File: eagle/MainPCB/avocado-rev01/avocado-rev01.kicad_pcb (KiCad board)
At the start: 4 copper layers, 61.5 x 59.8 mm, 110 parts, among them J1 10118194-0001LF, J3 0475710001, P2 camconn, U1 V3S, U2 AP65111A, U3 AP65111A, U4 AP65111A, U5 XC6206P302MR, X1 XTAL3.2X2, X2 XTAL5X1.9

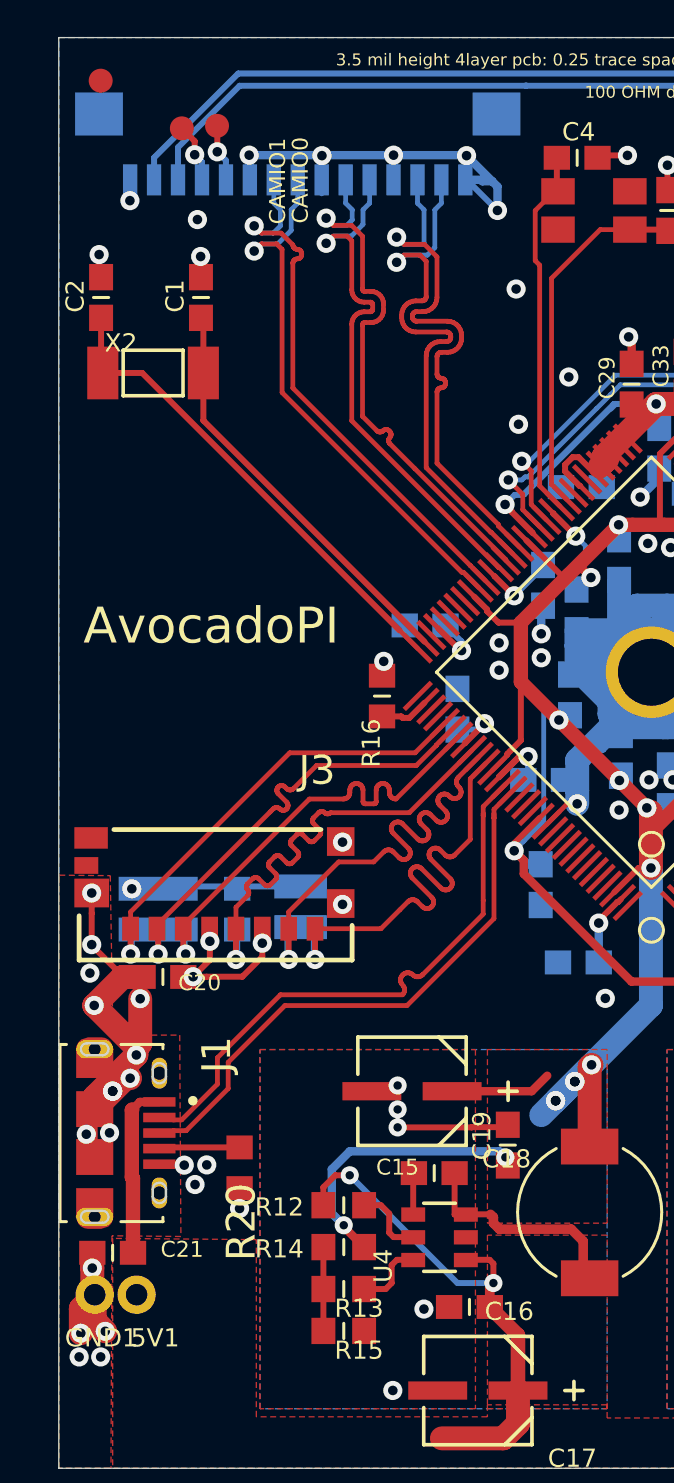
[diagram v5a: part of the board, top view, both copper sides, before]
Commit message: updated decoupling vias
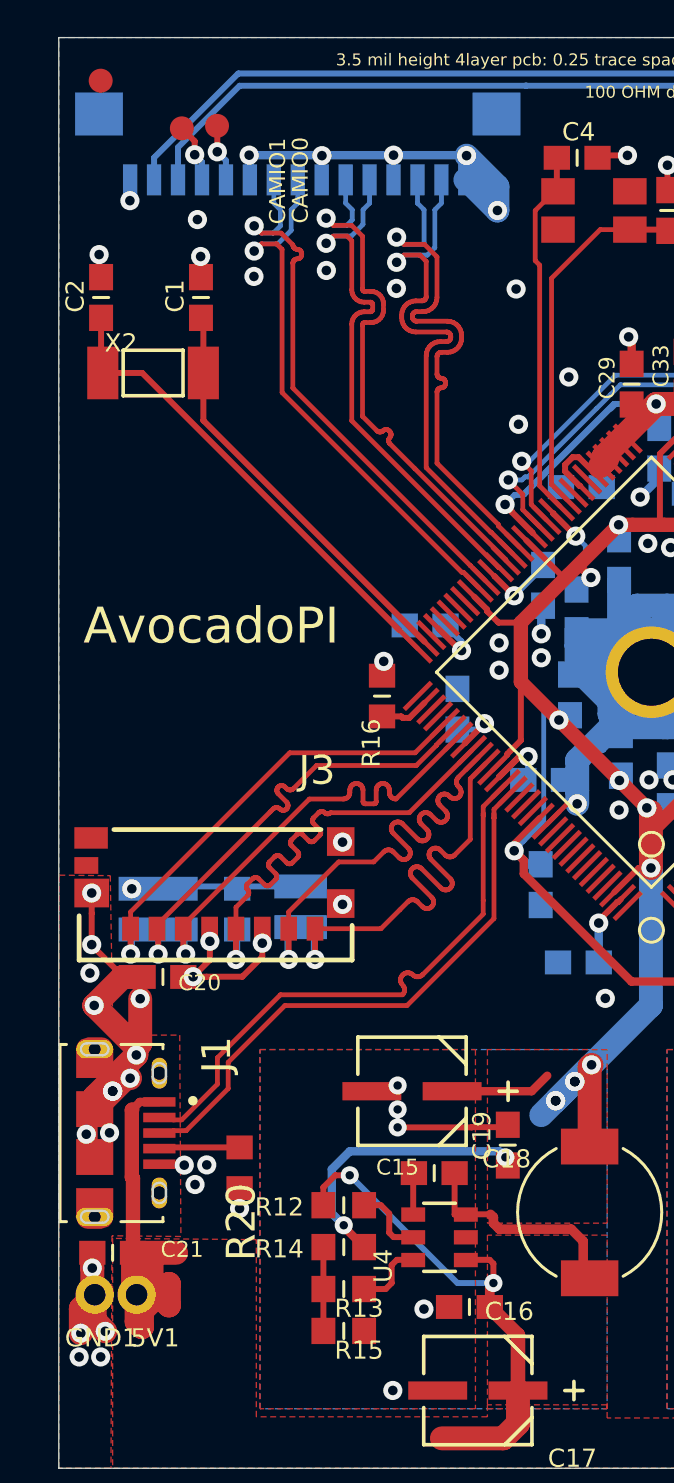
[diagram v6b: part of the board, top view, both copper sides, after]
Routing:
- net VCC: track 67.7 -> 78.4 mm
- net GND: track 150.5 -> 149.6 mm, vias 88 -> 91
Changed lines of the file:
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@@
-(kicad_pcb (version 20171130) (host pcbnew "(6.0.0-rc1-dev-1027-g90233e5ec)")
+(kicad_pcb (version 20171130) (host pcbnew "(5.0.2)-1")
   (general
     (thickness 1.6)
     (drawings 7)
-    (tracks 1809)
+    (tracks 1819)
     (zones 0)
     (modules 110)
@@
     (zone_45_only no)
     (trace_min 0.2)
+    (segment_width 0.2)
+    (edge_width 0.05)
     (via_size 0.8)
     (via_drill 0.4)
@@
     (uvia_min_size 0.2)
     (uvia_min_drill 0.1)
-    (edge_width 0.05)
-    (segment_width 0.2)
     (pcb_text_width 0.3)
     (pcb_text_size 1.5 1.5)
@@
   (via (at 135.85 85) (size 0.8) (drill 0.4) (layers Top Bottom) (net 1))
   (via (at 122.54 82.1) (size 0.8) (drill 0.4) (layers Top Bottom) (net 1))
-  (segment (start 127.73 80.44) (end 127.73 81) (width 0.25) (layer Bottom) (net 1))
   (segment (start 133.78 80.39) (end 133.73 80.44) (width 0.25) (layer Bottom) (net 1))
   (segment (start 133.78 79.43) (end 133.78 80.39) (width 0.25) (layer Bottom) (net 1))
-  (segment (start 133.79 80.44) (end 135.07 81.72) (width 0.25) (layer Bottom) (net 1))
-  (segment (start 133.73 80.44) (end 133.79 80.44) (width 0.25) (layer Bottom) (net 1))
   (segment (start 130.75 79.43) (end 130.73 79.41) (width 0.25) (layer Bottom) (net 1))
   (segment (start 133.78 79.43) (end 130.75 79.43) (width 0.25) (layer Bottom) (net 1))
@@
   (segment (start 133.76 79.41) (end 133.78 79.43) (width 0.35) (layer Bottom) (net 1))
   (segment (start 124.7 79.41) (end 133.76 79.41) (width 0.35) (layer Bottom) (net 1))
-  (segment (start 135.07 80.72) (end 135.07 81.72) (width 0.35) (layer Bottom) (net 1))
   (segment (start 134.44 80.5) (end 134.85 80.5) (width 0.35) (layer Bottom) (net 1))
-  (segment (start 134.38 80.44) (end 134.44 80.5) (width 0.35) (layer Bottom) (net 1))
-  (segment (start 133.73 80.44) (end 134.38 80.44) (width 0.35) (layer Bottom) (net 1))
-  (segment (start 133.78 79.43) (end 134.85 80.5) (width 0.35) (layer Bottom) (net 1))
   (segment (start 134.85 80.5) (end 135.07 80.72) (width 0.35) (layer Bottom) (net 1))
   (segment (start 141.825 92.895) (end 141.03 93.69) (width 0.35) (layer Bottom) (net 1))
@@
   (segment (start 158.925 112.9) (end 157.5 112.9) (width 0.35) (layer Top) (net 1))
   (via (at 156.15 112.825) (size 0.8) (drill 0.4) (layers Top Bottom) (net 1))
+  (via (at 130.85 84.975) (size 0.8) (drill 0.4) (layers Top Bottom) (net 1))
+  (via (at 127.925 84.225) (size 0.8) (drill 0.4) (layers Top Bottom) (net 1))
+  (via (at 124.9 84.475) (size 0.8) (drill 0.4) (layers Top Bottom) (net 1))
+  (segment (start 135.07 80.72) (end 133.78 79.43) (width 1) (layer Bottom) (net 1))
+  (segment (start 135.07 81.72) (end 135.07 80.72) (width 1) (layer Bottom) (net 1))
+  (segment (start 133.79 80.44) (end 135.07 81.72) (width 1) (layer Bottom) (net 1))
+  (segment (start 133.73 80.44) (end 133.79 80.44) (width 1) (layer Bottom) (net 1))
   (segment (start 145.8011 122.5136) (end 146.3011 122.0136) (width 0.25) (layer Top) (net 2))
   (via (at 146.9011 122.0136) (size 0.7564) (drill 0.35) (layers Top Bottom) (net 2))
@@
   (segment (start 171.9275 132.3846) (end 171.2621 133.05) (width 1) (layer Top) (net 2))
   (segment (start 171.9275 131.0036) (end 171.9275 132.3846) (width 1) (layer Top) (net 2))
+  (segment (start 119.85 126.85) (end 120 127) (width 1) (layer Top) (net 2))
+  (segment (start 119.85 125.25) (end 119.85 126.85) (width 1) (layer Top) (net 2))
+  (segment (start 120 128.13137) (end 120.225 128.35637) (width 1) (layer Top) (net 2))
+  (segment (start 120 127) (end 120 128.13137) (width 1) (layer Top) (net 2))
+  (segment (start 120.225 128.35637) (end 120.225 127.675) (width 1) (layer Top) (net 2))
+  (segment (start 120.225 127.675) (end 121.35 126.55) (width 1) (layer Top) (net 2))
+  (segment (start 121.35 126.55) (end 121.35 127.45) (width 1) (layer Top) (net 2))
+  (segment (start 121.35 127.45) (end 120.625 126.725) (width 1) (layer Top) (net 2))
+  (segment (start 120.625 126.725) (end 120.625 125.325) (width 1) (layer Top) (net 2))
+  (segment (start 119.85 125.25) (end 121.65 125.25) (width 1) (layer Top) (net 2))
   (via (at 122.36 113.72) (size 0.8) (drill 0.4) (layers Top Bottom) (net 3))
   (segment (start 165.5011 125.0136) (end 164.6511 124.1636) (width 0.35) (layer Top) (net 3))
@@
   (segment (start 122.425428 78.825428) (end 121.89 78.29) (width 0.25) (layer Top) (net 18))
   (segment (start 122.425428 79.39188) (end 122.425428 78.825428) (width 0.25) (layer Top) (net 18))
-  (via (at 138.34 95.32) (size 0.8) (drill 0.4) (layers Top Bottom) (net 68))
-  (segment (start 137.399881 94.356796) (end 137.399881 94.379881) (width 0.25) (layer Top) (net 68))
-  (segment (start 137.399881 94.379881) (end 138.34 95.32) (width 0.25) (layer Top) (net 68))
-  (via (at 135.768795 108.461323) (size 0.8) (drill 0.4) (layers Top Bottom) (net 68))
-  (segment (start 136.834195 107.084718) (end 135.768795 108.150118) (width 0.25) (layer Top) (net 68))
-  (segment (start 135.768795 108.150118) (end 135.768795 108.461323) (width 0.25) (layer Top) (net 68))
-  (segment (start 138.739999 95.719999) (end 138.739999 96.060001) (width 0.2) (layer Bottom) (net 68))
-  (segment (start 138.34 95.32) (end 138.739999 95.719999) (width 0.2) (layer Bottom) (net 68))
-  (segment (start 138.739999 96.060001) (end 136.2 98.6) (width 0.2) (layer Bottom) (net 68))
-  (segment (start 136.2 98.6) (end 136.2 101.5) (width 0.2) (layer Bottom) (net 68))
-  (segment (start 136.168794 108.061324) (end 135.768795 108.461323) (width 0.2) (layer Bottom) (net 68))
-  (segment (start 137.002401 107.227717) (end 136.168794 108.061324) (width 0.2) (layer Bottom) (net 68))
-  (segment (start 137.002401 102.302401) (end 137.002401 107.227717) (width 0.2) (layer Bottom) (net 68))
-  (segment (start 136.2 101.5) (end 137.002401 102.302401) (width 0.2) (layer Bottom) (net 68))
   (segment (start 131.05 102.85) (end 130.25 102.85) (width 0.25) (layer Top) (net 19))
   (segment (start 131.112787 102.912787) (end 131.05 102.85) (width 0.25) (layer Top) (net 19))
@@
   (segment (start 131.833099 113.707929) (end 131.891839 113.679642) (width 0.2) (layer Top) (net 67))
   (segment (start 131.891839 113.679642) (end 131.942811 113.638992) (width 0.2) (layer Top) (net 67))
+  (via (at 138.34 95.32) (size 0.8) (drill 0.4) (layers Top Bottom) (net 68))
+  (segment (start 137.399881 94.356796) (end 137.399881 94.379881) (width 0.25) (layer Top) (net 68))
+  (segment (start 137.399881 94.379881) (end 138.34 95.32) (width 0.25) (layer Top) (net 68))
+  (via (at 135.768795 108.461323) (size 0.8) (drill 0.4) (layers Top Bottom) (net 68))
+  (segment (start 136.834195 107.084718) (end 135.768795 108.150118) (width 0.25) (layer Top) (net 68))
+  (segment (start 135.768795 108.150118) (end 135.768795 108.461323) (width 0.25) (layer Top) (net 68))
+  (segment (start 138.739999 95.719999) (end 138.739999 96.060001) (width 0.2) (layer Bottom) (net 68))
+  (segment (start 138.34 95.32) (end 138.739999 95.719999) (width 0.2) (layer Bottom) (net 68))
+  (segment (start 138.739999 96.060001) (end 136.2 98.6) (width 0.2) (layer Bottom) (net 68))
+  (segment (start 136.2 98.6) (end 136.2 101.5) (width 0.2) (layer Bottom) (net 68))
+  (segment (start 136.168794 108.061324) (end 135.768795 108.461323) (width 0.2) (layer Bottom) (net 68))
+  (segment (start 137.002401 107.227717) (end 136.168794 108.061324) (width 0.2) (layer Bottom) (net 68))
+  (segment (start 137.002401 102.302401) (end 137.002401 107.227717) (width 0.2) (layer Bottom) (net 68))
+  (segment (start 136.2 101.5) (end 137.002401 102.302401) (width 0.2) (layer Bottom) (net 68))
   (segment (start 157.6 114.8) (end 157.45 114.65) (width 0.35) (layer Top) (net 68))
   (segment (start 158.925 114.8) (end 157.6 114.8) (width 0.35) (layer Top) (net 68))
@@
     (polygon
       (pts
-        (xy 121.71 81.1) (xy 136.05 81.0775) (xy 136.99 82.8425) (xy 136.73 85.795) (xy 121.66 85.76)
+        (xy 121.71 81.1) (xy 136.05 81.0775) (xy 136.99 82.8425) (xy 136.73 86.3775) (xy 121.66 86.3425)
       )
     )
@@
     (polygon
       (pts
-        (xy 136.58 85.83) (xy 122.13 85.65) (xy 121.95 87.13) (xy 136.6 87.3) (xy 136.58 85.81)
+        (xy 136.58 86.45) (xy 122.13 86.27) (xy 121.95 87.13) (xy 136.6 87.3) (xy 136.58 85.81)
       )
     )

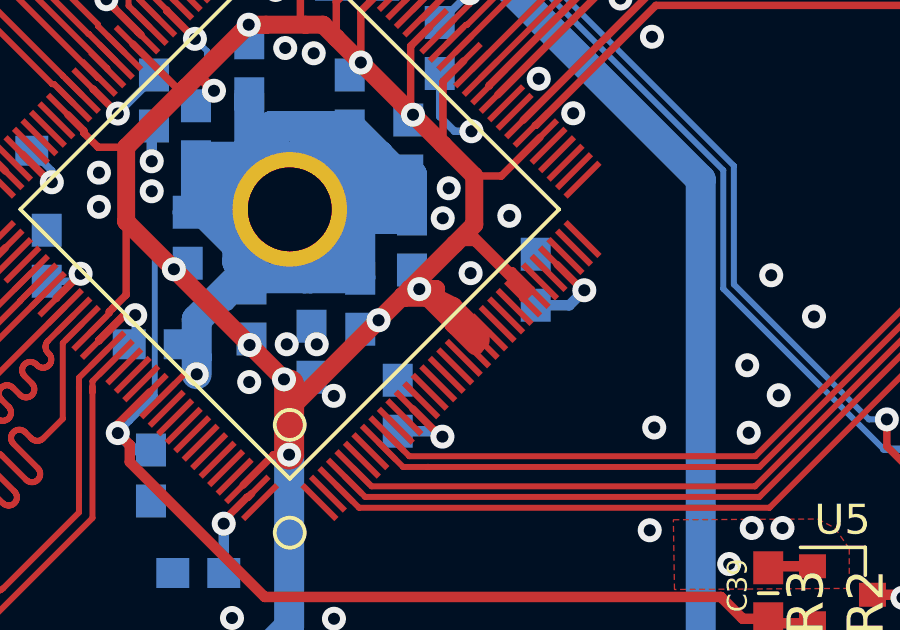
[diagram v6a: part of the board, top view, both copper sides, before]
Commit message: update keepout area
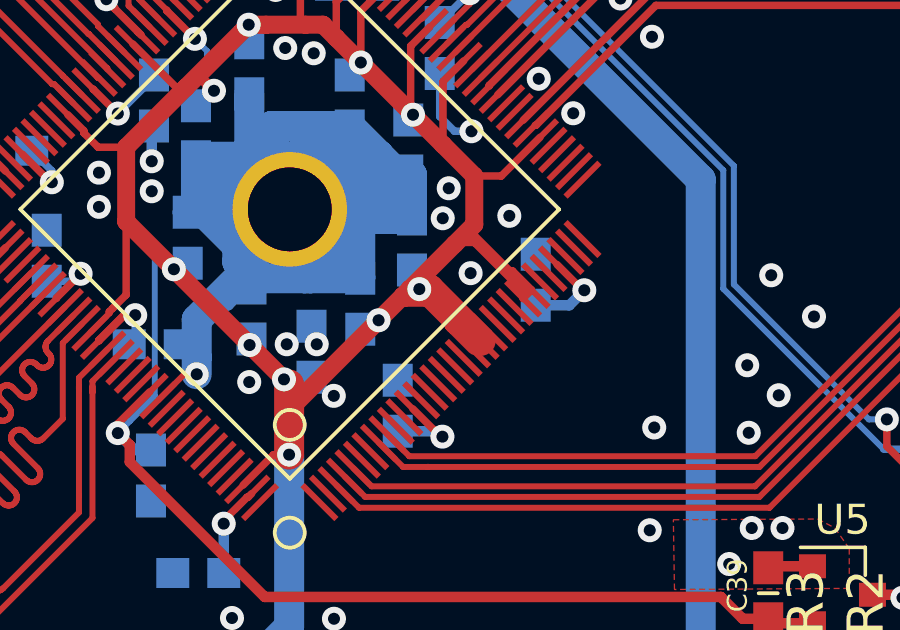
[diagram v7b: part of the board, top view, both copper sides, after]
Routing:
- net 1V2: track 126.6 -> 128.2 mm
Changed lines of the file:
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@@
   (segment (start 147.865061 105.146241) (end 146.95 104.23118) (width 0.6) (layer Top) (net 5))
   (segment (start 146.95 104.822743) (end 146.95 104.791554) (width 0.6) (layer Top) (net 5))
-  (segment (start 146.380374 103.661554) (end 145.82 103.661554) (width 0.6) (layer Top) (net 5))
   (segment (start 145.82 103.661554) (end 145.5 103.661554) (width 0.6) (layer Top) (net 5))
   (segment (start 145.328446 103.95) (end 145.27 103.891554) (width 0.6) (layer Top) (net 5))
@@
   (segment (start 145.61 97.848446) (end 145.61 97.848446) (width 0.25) (layer Top) (net 5))
   (via (at 145.61 97.848446) (size 0.8) (drill 0.4) (layers Top Bottom) (net 5))
-  (segment (start 145.82 103.661554) (end 146.380374 103.661554) (width 0.6) (layer Top) (net 5))
   (via (at 145.82 103.661554) (size 0.8) (drill 0.4) (layers Top Bottom) (net 5))
   (segment (start 144.461554 104.7) (end 145.27 103.891554) (width 0.6) (layer Top) (net 5))
@@
   (segment (start 142.155 106.67) (end 142.225 106.6) (width 0.25) (layer Bottom) (net 5))
   (segment (start 141.308446 106.67) (end 142.155 106.67) (width 0.25) (layer Bottom) (net 5))
+  (segment (start 146.138953 103.661554) (end 147.865061 105.387662) (width 1) (layer Top) (net 5))
+  (segment (start 145.82 103.661554) (end 146.138953 103.661554) (width 1) (layer Top) (net 5))
   (segment (start 167.5511 105.6536) (end 167.6011 105.6536) (width 0.2) (layer Top) (net 6))
   (segment (start 166.3575 104.46) (end 167.5511 105.6536) (width 0.2) (layer Top) (net 6))
@@
     (polygon
       (pts
-        (xy 124.05 81.19) (xy 124.07 79.72) (xy 134.14 79.74) (xy 134.15 81.18)
+        (xy 124.025 81.08) (xy 124.07 79.72) (xy 134.14 79.74) (xy 134.125 81.07)
       )
     )
@@
     (polygon
       (pts
-        (xy 121.56 80.44) (xy 134.29 80.38) (xy 138.025 80.43) (xy 137.975 81.25) (xy 121.54 81.39)
-        (xy 121.57 80.41) (xy 121.57 80.44)
-      )
-    )
-  )
-  (zone (net 0) (net_name "") (layer In2.Cu) (hatch edge 0.508)
-    (connect_pads (clearance 0.508))
-    (min_thickness 0.254)
-    (keepout (tracks allowed) (vias allowed) (copperpour not_allowed))
-    (fill (arc_segments 16) (thermal_gap 0.508) (thermal_bridge_width 0.508))
-    (polygon
-      (pts
-        (xy 136.58 86.45) (xy 122.13 86.27) (xy 121.95 87.13) (xy 136.6 87.3) (xy 136.58 85.81)
-      )
-    )
-  )
-  (zone (net 0) (net_name "") (layer In2.Cu) (hatch edge 0.508)
-    (connect_pads (clearance 0.508))
-    (min_thickness 0.254)
-    (keepout (tracks allowed) (vias allowed) (copperpour not_allowed))
-    (fill (arc_segments 16) (thermal_gap 0.508) (thermal_bridge_width 0.508))
-    (polygon
-      (pts
-        (xy 121.55 80.41) (xy 120.69 80.42) (xy 120.63 87.07) (xy 122.08 87.13) (xy 122.18 85.54)
-        (xy 121.5 85.54) (xy 121.58 80.41) (xy 121.56 80.41)
+        (xy 138.025 80.43) (xy 138.0175 80.98) (xy 121.5825 81.12) (xy 121.575303 80.711208) (xy 121.5 85.54)
+        (xy 122.18 85.54) (xy 122.134085 86.270051) (xy 136.58 86.45) (xy 136.58 85.81) (xy 136.6 87.3)
+        (xy 121.95 87.13) (xy 121.951116 87.124667) (xy 120.63 87.07) (xy 120.69 80.42) (xy 121.55 80.41)
+        (xy 121.58 80.41) (xy 121.579534 80.439908) (xy 134.29 80.38)
       )
     )
@@
       )
     )
+  )
+  (zone (net 0) (net_name "") (layer In2.Cu) (hatch edge 0.508)
+    (connect_pads (clearance 0.508))
+    (min_thickness 0.254)
+    (keepout (tracks allowed) (vias allowed) (copperpour not_allowed))
+    (fill (arc_segments 16) (thermal_gap 0.508) (thermal_bridge_width 0.508))
+    (polygon
+      (pts
+        (xy 121.57 80.44) (xy 121.56 80.44) (xy 121.57 80.439953)
+      )
+    )
+  )
+  (zone (net 0) (net_name "") (layer In2.Cu) (hatch edge 0.508)
+    (connect_pads (clearance 0.508))
+    (min_thickness 0.254)
+    (keepout (tracks allowed) (vias allowed) (copperpour not_allowed))
+    (fill (arc_segments 16) (thermal_gap 0.508) (thermal_bridge_width 0.508))
+    (polygon
+      (pts
+        (xy 121.57 80.41) (xy 121.570527 80.43995) (xy 121.57 80.439953)
+      )
+    )
